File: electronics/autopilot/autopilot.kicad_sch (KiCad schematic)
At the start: 29 parts, among them J1 SERVO, J10 MPPT_I2C, J11 Debug, J12 5V IN, J13 Vbatt, J2 SERVO, J3 SERVO, J4 SERVO, J5 ESC, J6 GSM_MODULE, J7 IBUS, J8 5V IN, J9 IMU, U1 Pico, U2 SIM28ML, U3 NRF24L01_Breakout, U4 74HC244

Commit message: new model
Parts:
- added SW1: ARM, Connector_PinHeader_2.54mm:PinHeader_1x02_P2.54mm_Vertical, symbol Switch:SW_DIP_x01
- J12: value 5V IN -> 3.3V IN
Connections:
- net GND: now also SW1.1
- net arm: now reaches U1.5 (GPIO3)
- net arm: now also SW1.2
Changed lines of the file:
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@@
+    (stroke (width 0) (type default) (color 0 0 0 0))
+  )
+  (wire (pts (xy 120.65 43.18) (xy 124.46 43.18))
     (stroke (width 0) (type default) (color 0 0 0 0))
   )
@@
     (stroke (width 0) (type default) (color 0 0 0 0))
   )
+  (wire (pts (xy 165.1 111.76) (xy 165.1 114.3))
+    (stroke (width 0) (type default) (color 0 0 0 0))
+  )
   (wire (pts (xy 160.02 66.04) (xy 163.83 66.04))
     (stroke (width 0) (type default) (color 0 0 0 0))
@@
     (stroke (width 0) (type default) (color 0 0 0 0))
   )
+  (wire (pts (xy 165.1 129.54) (xy 165.1 132.08))
+    (stroke (width 0) (type default) (color 0 0 0 0))
+  )
   (wire (pts (xy 119.38 81.28) (xy 124.46 81.28))
     (stroke (width 0) (type default) (color 0 0 0 0))
@@
     (effects (font (size 1.27 1.27)) (justify left bottom))
   )
+  (label "arm" (at 120.65 43.18 0)
+    (effects (font (size 1.27 1.27)) (justify left bottom))
+  )
   (label "CE" (at 163.83 78.74 0)
     (effects (font (size 1.27 1.27)) (justify left bottom))
@@
   )
   (label "IMU_I2C_SCL" (at 110.49 105.41 0)
+    (effects (font (size 1.27 1.27)) (justify left bottom))
+  )
+  (label "arm" (at 165.1 111.76 0)
     (effects (font (size 1.27 1.27)) (justify left bottom))
   )
@@
     )
     (pin "1")
+  )
+  (symbol (lib_id "power:GND") (at 165.1 132.08 0) (unit 1)
+    (in_bom yes) (on_board yes) (fields_autoplaced)
+    (property "Reference" "#PWR0102" (id 0) (at 165.1 138.43 0)
+      (effects (font (size 1.27 1.27)) hide)
+    )
+    (property "Value" "GND" (id 1) (at 165.1 137.16 0))
+    (property "Footprint" "" (id 2) (at 165.1 132.08 0)
+      (effects (font (size 1.27 1.27)) hide)
+    )
+    (property "Datasheet" "" (id 3) (at 165.1 132.08 0)
+      (effects (font (size 1.27 1.27)) hide)
+    )
+    (pin "1")
+  )
+  (symbol (lib_id "Switch:SW_DIP_x01") (at 165.1 121.92 90) (unit 1)
+    (in_bom yes) (on_board yes) (fields_autoplaced)
+    (property "Reference" "SW1" (id 0) (at 168.91 120.6499 90)
+      (effects (font (size 1.27 1.27)) (justify right))
+    )
+    (property "Value" "ARM" (id 1) (at 168.91 123.1899 90)
+      (effects (font (size 1.27 1.27)) (justify right))
+    )
+    (property "Footprint" "Connector_PinHeader_2.54mm:PinHeader_1x02_P2.54mm_Vertical" (id 2) (at 165.1 121.92 0)
+      (effects (font (size 1.27 1.27)) hide)
+    )
+    (property "Datasheet" "~" (id 3) (at 165.1 121.92 0)
+      (effects (font (size 1.27 1.27)) hide)
+    )
+    (pin "1")
+    (pin "2")
   )
   (symbol (lib_id "Connector:Conn_01x03_Male") (at 26.67 69.85 0) (unit 1)
@@
     (in_bom yes) (on_board yes) (fields_autoplaced)
     (property "Reference" "J12" (id 0) (at 58.42 85.09 0))
-    (property "Value" "5V IN" (id 1) (at 58.42 87.63 0))
+    (property "Value" "3.3V IN" (id 1) (at 58.42 87.63 0))
     (property "Footprint" "moje:ARK" (id 2) (at 58.42 91.44 0)
       (effects (font (size 1.27 1.27)) hide)
@@
       (reference "#PWR0101") (unit 1) (value "GND") (footprint "")
     )
+    (path "/7b63db0e-163d-4874-be63-a364f26c4fb5"
+      (reference "#PWR0102") (unit 1) (value "GND") (footprint "")
+    )
     (path "/31a915df-d94a-4c5d-a919-8d4fe132c8c9"
       (reference "AE1") (unit 1) (value "Antenna") (footprint "Connector_PinHeader_2.54mm:PinHeader_1x01_P2.54mm_Vertical")
@@
     )
     (path "/af55ffb3-a8ad-455d-ad63-1cae0c75ac50"
-      (reference "J12") (unit 1) (value "5V IN") (footprint "moje:ARK")
+      (reference "J12") (unit 1) (value "3.3V IN") (footprint "moje:ARK")
     )
     (path "/710045fb-f91b-414f-844b-e32080368dd7"
@@
       (reference "R6") (unit 1) (value "10") (footprint "Resistor_SMD:R_1206_3216Metric_Pad1.30x1.75mm_HandSolder")
     )
+    (path "/7c2480f6-24ef-4833-bcb5-b898217a57a5"
+      (reference "SW1") (unit 1) (value "ARM") (footprint "Connector_PinHeader_2.54mm:PinHeader_1x02_P2.54mm_Vertical")
+    )
     (path "/c88a519f-e61a-4dab-852f-52e9f8605296"

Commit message: autopilot rework
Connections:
- net GPS_RST renamed GMS_RST
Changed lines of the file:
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@@
     (effects (font (size 1.27 1.27)) (justify right bottom))
   )
-  (label "GPS_RST" (at 102.87 171.45 0)
+  (label "GMS_RST" (at 102.87 171.45 0)
     (effects (font (size 1.27 1.27)) (justify left bottom))
   )
@@
     (effects (font (size 1.27 1.27)) (justify right bottom))
   )
-  (label "GPS_RST" (at 119.38 40.64 180)
+  (label "GMS_RST" (at 119.38 40.64 180)
     (effects (font (size 1.27 1.27)) (justify right bottom))
   )

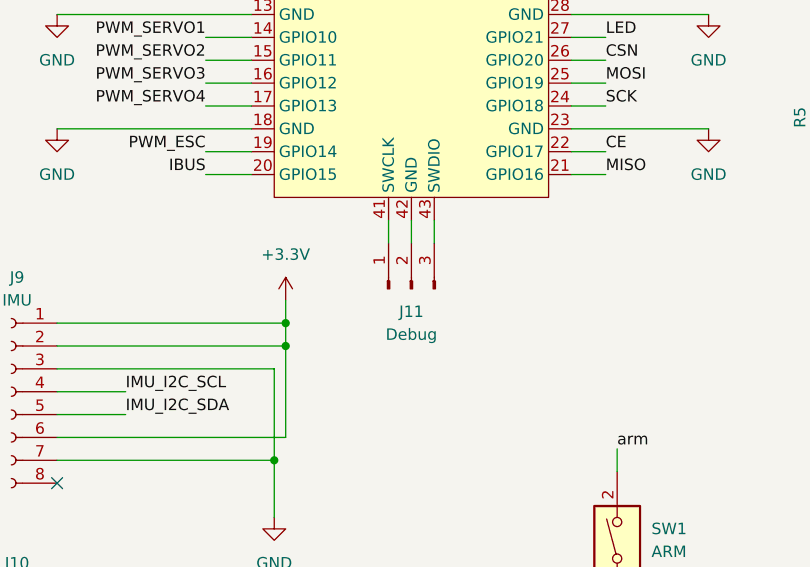
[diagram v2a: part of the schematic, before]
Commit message: autopilot buffer footprint fixed
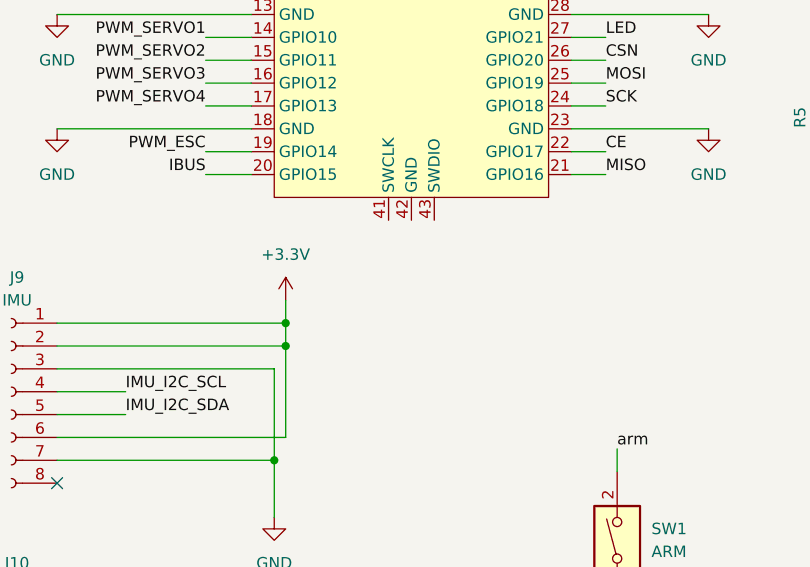
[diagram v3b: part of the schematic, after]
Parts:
- removed J11: Debug, Connector_PinHeader_2.54mm:PinHeader_1x03_P2.54mm_Vertical, symbol Connector:Conn_01x03_Male
- U4: footprint Package_SO:HTSSOP-20-1EP_4.4x6.5mm_P0.65mm_EP2.85x4mm -> Package_SO:SO-20_12.8x7.5mm_P1.27mm
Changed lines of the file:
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@@
-    (stroke (width 0) (type default) (color 0 0 0 0))
-  )
-  (wire (pts (xy 144.78 86.36) (xy 144.78 88.9))
     (stroke (width 0) (type default) (color 0 0 0 0))
   )
@@
     (stroke (width 0) (type default) (color 0 0 0 0))
   )
-  (wire (pts (xy 139.7 86.36) (xy 139.7 88.9))
-    (stroke (width 0) (type default) (color 0 0 0 0))
-  )
   (wire (pts (xy 264.16 38.1) (xy 264.16 39.37))
     (stroke (width 0) (type default) (color 0 0 0 0))
@@
   )
   (wire (pts (xy 248.92 30.48) (xy 248.92 29.21))
-    (stroke (width 0) (type default) (color 0 0 0 0))
-  )
-  (wire (pts (xy 142.24 86.36) (xy 142.24 88.9))
     (stroke (width 0) (type default) (color 0 0 0 0))
   )
@@
       (effects (font (size 1.27 1.27)) (justify left))
     )
-    (property "Footprint" "Package_SO:HTSSOP-20-1EP_4.4x6.5mm_P0.65mm_EP2.85x4mm" (id 2) (at 49.53 151.13 0)
+    (property "Footprint" "Package_SO:SO-20_12.8x7.5mm_P1.27mm" (id 2) (at 49.53 151.13 0)
       (effects (font (size 1.27 1.27)) hide)
     )
@@
     (pin "2")
   )
-  (symbol (lib_id "Connector:Conn_01x03_Male") (at 142.24 93.98 90) (unit 1)
-    (in_bom yes) (on_board yes) (fields_autoplaced)
-    (property "Reference" "J11" (id 0) (at 142.24 96.52 90))
-    (property "Value" "Debug" (id 1) (at 142.24 99.06 90))
-    (property "Footprint" "Connector_PinHeader_2.54mm:PinHeader_1x03_P2.54mm_Vertical" (id 2) (at 142.24 93.98 0)
-      (effects (font (size 1.27 1.27)) hide)
-    )
-    (property "Datasheet" "~" (id 3) (at 142.24 93.98 0)
-      (effects (font (size 1.27 1.27)) hide)
-    )
-    (pin "1")
-    (pin "2")
-    (pin "3")
-  )
   (symbol (lib_id "Device:C_Small") (at 240.03 25.4 0) (unit 1)
     (in_bom yes) (on_board yes) (fields_autoplaced)
@@
       (reference "J10") (unit 1) (value "MPPT_I2C") (footprint "Connector_PinHeader_2.54mm:PinHeader_1x03_P2.54mm_Vertical")
     )
-    (path "/da184c56-6b22-4ce8-9a84-ce9c8348e205"
-      (reference "J11") (unit 1) (value "Debug") (footprint "Connector_PinHeader_2.54mm:PinHeader_1x03_P2.54mm_Vertical")
-    )
     (path "/af55ffb3-a8ad-455d-ad63-1cae0c75ac50"
       (reference "J12") (unit 1) (value "3.3V IN") (footprint "moje:ARK")
@@
     )
     (path "/b615f88e-fbeb-40c2-9372-43ac60f3028c"
-      (reference "U4") (unit 1) (value "74HC244") (footprint "Package_SO:HTSSOP-20-1EP_4.4x6.5mm_P0.65mm_EP2.85x4mm")
-    )
-  )
+      (reference "U4") (unit 1) (value "74HC244") (footprint "Package_SO:SO-20_12.8x7.5mm_P1.27mm")
+    )
+  )

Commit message: small fixes
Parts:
- removed AE1: Antenna, Connector_PinHeader_2.54mm:PinHeader_1x01_P2.54mm_Vertical, symbol Device:Antenna
- added J11: Antena, Connector_Coaxial:U.FL_Molex_MCRF_73412-0110_Vertical, symbol Samolot:ULF
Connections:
- net GND: now also J11.2 (Shield)
- net at L1.2, U2.11 (RF_IN): now also J11.1 (Pin_1)
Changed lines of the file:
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@@
+    (stroke (width 0) (type default) (color 0 0 0 0))
+  )
+  (wire (pts (xy 279.4 62.23) (xy 279.4 57.15))
     (stroke (width 0) (type default) (color 0 0 0 0))
   )
@@
   )
   (wire (pts (xy 99.06 163.83) (xy 102.87 163.83))
-    (stroke (width 0) (type default) (color 0 0 0 0))
-  )
-  (wire (pts (xy 274.32 50.8) (xy 274.32 52.07))
     (stroke (width 0) (type default) (color 0 0 0 0))
   )
@@
     (pin "1")
   )
-  (symbol (lib_id "Device:Antenna") (at 274.32 45.72 0) (unit 1)
-    (in_bom yes) (on_board yes) (fields_autoplaced)
-    (property "Reference" "AE1" (id 0) (at 276.86 45.0849 0)
-      (effects (font (size 1.27 1.27)) (justify left))
-    )
-    (property "Value" "Antenna" (id 1) (at 276.86 47.6249 0)
-      (effects (font (size 1.27 1.27)) (justify left))
-    )
-    (property "Footprint" "Connector_PinHeader_2.54mm:PinHeader_1x01_P2.54mm_Vertical" (id 2) (at 274.32 45.72 0)
-      (effects (font (size 1.27 1.27)) hide)
-    )
-    (property "Datasheet" "https://www.tme.eu/pl/details/gps-ant050-7/anteny-gps/sr-passives/gps-ant050/" (id 3) (at 274.32 45.72 0)
-      (effects (font (size 1.27 1.27)) hide)
-    )
-    (pin "1")
-  )
   (symbol (lib_id "power:GND") (at 38.1 91.44 0) (unit 1)
     (in_bom yes) (on_board yes) (fields_autoplaced)
@@
     )
     (property "Datasheet" "" (id 3) (at 175.26 38.1 0)
+      (effects (font (size 1.27 1.27)) hide)
+    )
+    (pin "1")
+  )
+  (symbol (lib_id "power:GND") (at 279.4 62.23 0) (unit 1)
+    (in_bom yes) (on_board yes) (fields_autoplaced)
+    (property "Reference" "#PWR040" (id 0) (at 279.4 68.58 0)
+      (effects (font (size 1.27 1.27)) hide)
+    )
+    (property "Value" "GND" (id 1) (at 279.4 67.31 0))
+    (property "Footprint" "" (id 2) (at 279.4 62.23 0)
+      (effects (font (size 1.27 1.27)) hide)
+    )
+    (property "Datasheet" "" (id 3) (at 279.4 62.23 0)
       (effects (font (size 1.27 1.27)) hide)
     )
@@
     )
     (property "Datasheet" "https://www.tme.eu/pl/details/mr12x10r0ftl/rezystory-smd-1206/walsin/" (id 3) (at 257.81 38.1 0)
+      (effects (font (size 1.27 1.27)) hide)
+    )
+    (pin "1")
+    (pin "2")
+  )
+  (symbol (lib_id "Samolot:ULF") (at 279.4 52.07 0) (unit 1)
+    (in_bom yes) (on_board yes) (fields_autoplaced)
+    (property "Reference" "J11" (id 0) (at 281.94 50.7999 0)
+      (effects (font (size 1.27 1.27)) (justify left))
+    )
+    (property "Value" "Antena" (id 1) (at 281.94 53.3399 0)
+      (effects (font (size 1.27 1.27)) (justify left))
+    )
+    (property "Footprint" "Connector_Coaxial:U.FL_Molex_MCRF_73412-0110_Vertical" (id 2) (at 279.4 52.07 0)
+      (effects (font (size 1.27 1.27)) hide)
+    )
+    (property "Datasheet" "https://www.tme.eu/pl/details/gps-ant050-7/anteny-gps/sr-passives/gps-ant050/" (id 3) (at 279.4 52.07 0)
       (effects (font (size 1.27 1.27)) hide)
     )
@@
       (reference "#PWR039") (unit 1) (value "GND") (footprint "")
     )
+    (path "/7a4813b0-fa33-4bb5-9f6b-c2e4e0a664d7"
+      (reference "#PWR040") (unit 1) (value "GND") (footprint "")
+    )
     (path "/4a8b7425-4083-48cc-83b6-e622cb8f6444"
       (reference "#PWR0101") (unit 1) (value "GND") (footprint "")
@@
       (reference "#PWR0102") (unit 1) (value "GND") (footprint "")
     )
-    (path "/31a915df-d94a-4c5d-a919-8d4fe132c8c9"
-      (reference "AE1") (unit 1) (value "Antenna") (footprint "Connector_PinHeader_2.54mm:PinHeader_1x01_P2.54mm_Vertical")
-    )
     (path "/da9851f9-2be8-48ce-b766-4b208b5fe703"
       (reference "C1") (unit 1) (value "100n") (footprint "Capacitor_SMD:C_1206_3216Metric_Pad1.33x1.80mm_HandSolder")
@@
       (reference "J10") (unit 1) (value "MPPT_I2C") (footprint "Connector_PinHeader_2.54mm:PinHeader_1x03_P2.54mm_Vertical")
     )
+    (path "/bd91918a-d93b-4ce7-aac0-3d2ae87b6b78"
+      (reference "J11") (unit 1) (value "Antena") (footprint "Connector_Coaxial:U.FL_Molex_MCRF_73412-0110_Vertical")
+    )
     (path "/af55ffb3-a8ad-455d-ad63-1cae0c75ac50"
